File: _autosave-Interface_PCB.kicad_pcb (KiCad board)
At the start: 2 copper layers, 35 parts, among them IC1 STM32L412RBT6P, J1 USB_B, J2 AVR-JTAG-10, J3 Conn_01x04, J4 Conn_01x04, J5 Conn_01x04, J6 Conn_01x04, J7 Micro_SD_Card, U1 AMS1117-3.3

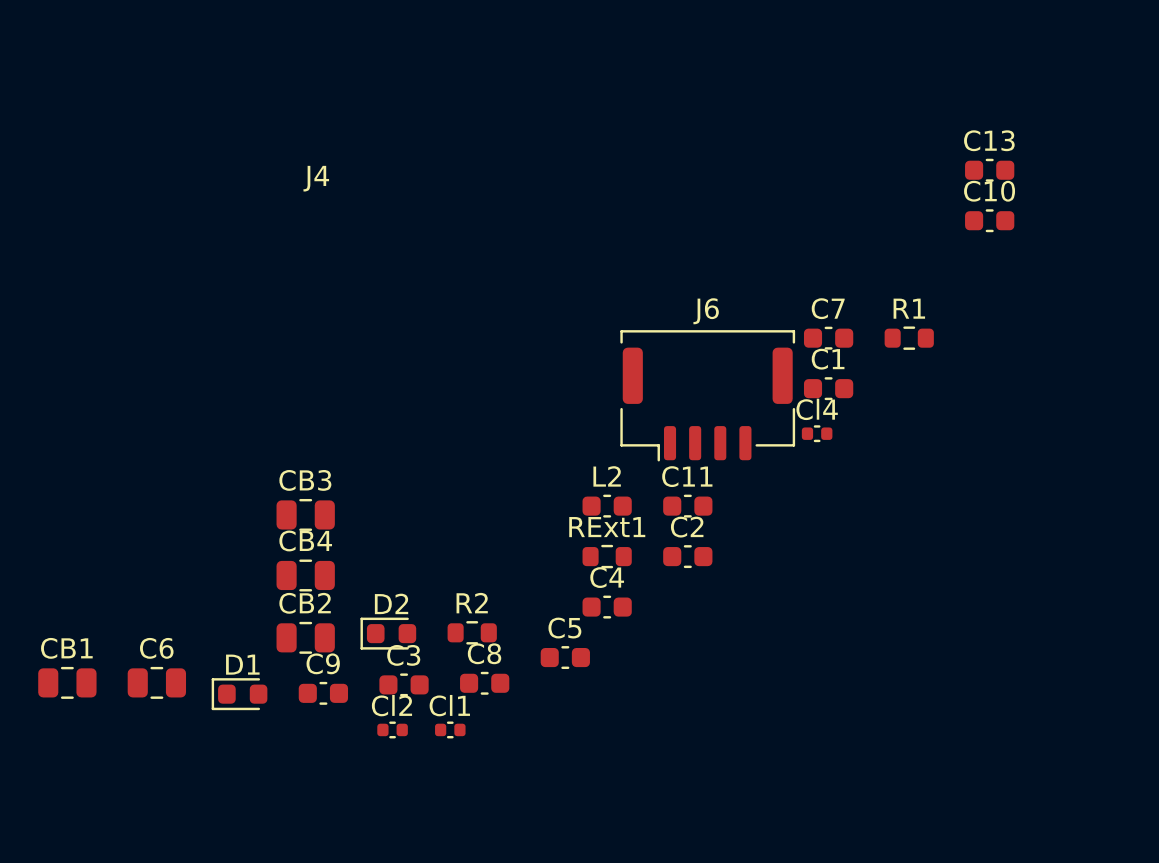
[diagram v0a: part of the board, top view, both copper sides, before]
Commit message: README added
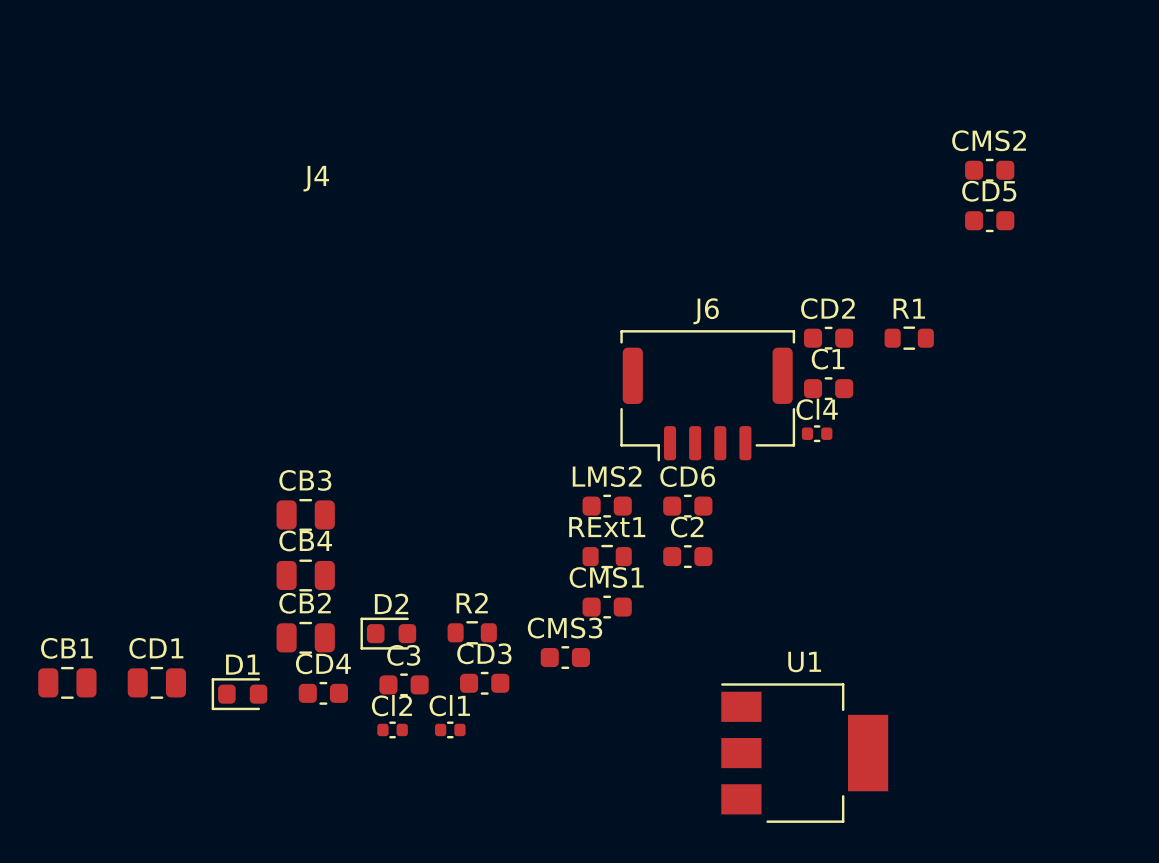
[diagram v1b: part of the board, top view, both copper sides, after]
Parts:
- added U1: AMS1117-3.3, Package_TO_SOT_SMD:SOT-223-3_TabPin2, F.Cu at (99.1, 119.4)
- renumbered C6 to CD1, C7 to CD2, C8 to CD3, C9 to CD4, C10 to CD5, C11 to CD6, C4 to CMS1, C13 to CMS2, C5 to CMS3, L2 to LMS2

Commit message: Added all component links and modified the footprints
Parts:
- removed the U1 at (99.1, 119.4)
- added CD1: 4.7u, Capacitor_SMD:C_0402_1005Metric, F.Cu at (129.5, 106.7)
- added CD2: 100n, Capacitor_SMD:C_0805_2012Metric, F.Cu at (133.3, 109.4)
- added CD3: 100n, Capacitor_SMD:C_0805_2012Metric, F.Cu at (133.8, 106.4)
- added CD4: 100n, Capacitor_SMD:C_0805_2012Metric, F.Cu at (129.3, 109.4)
- added CD5: 100n, Capacitor_SMD:C_0805_2012Metric, F.Cu at (125.5, 115.2)
- added CD6: 100n, Capacitor_SMD:C_0805_2012Metric, F.Cu at (129.5, 114.5)
- added CMS1: 10n, Capacitor_SMD:C_0805_2012Metric, F.Cu at (137.8, 106.4)
- added CMS2: 1u, Capacitor_SMD:C_0805_2012Metric, F.Cu at (133.5, 112.0)
- added CMS3: 10n, Capacitor_SMD:C_0805_2012Metric, F.Cu at (129.5, 112.0)
- added CR1: 22uF, Capacitor_SMD:C_0402_1005Metric, F.Cu at (68.6, 58.4)
- added CR2: 22uF, Capacitor_SMD:C_0402_1005Metric, F.Cu at (65.7, 60.4)
- added CR3: 22uF, Capacitor_SMD:C_0402_1005Metric, F.Cu at (77.2, 54.9)
- added CSD1: 0.1uF, Capacitor_SMD:C_0402_1005Metric, F.Cu at (77.2, 56.8)
- added LMS1: 39nH, Capacitor_SMD:C_0603_1608Metric, F.Cu at (125.5, 112.7)
- added LR1: 39nH, Inductor_SMD:L_0402_1005Metric, F.Cu at (65.7, 58.4)
- added NT1: NetTie_3_Tee, NetTie:NetTie-3_SMD_Pad2.0mm, F.Cu at (70.0, 55.7)
- added Y1: Crystal, SamacSys_Parts:ABS05W32768KHZD2T, F.Cu at (121.2, 113.5)
- added Y2: Crystal, SamacSys_Parts:ECS80830QVSTR, F.Cu at (122.8, 108.3)
- CB1, CB2, CB3: footprint Capacitor_SMD:C_0805_2012Metric -> Capacitor_SMD:C_0402_1005Metric
- D1, D2: footprint LED_SMD:LED_0603_1608Metric -> LED_SMD:LED_0805_2012Metric
- IC1: footprint STM32L412RBT6P:QFP50P1200X1200X160-64N -> SamacSys_Parts:QFP50P1200X1200X160-64N
- J1: value USB_B -> Conn_01x04; footprint Connector_USB:USB_Micro-B_Amphenol_10104110_Horizontal -> SamacSys_Parts:502382-0470
- J2: value AVR-JTAG-10 -> Conn_01x04; footprint Connector_PinHeader_2.54mm:PinHeader_2x05_P2.54mm_Vertical_SMD -> SamacSys_Parts:502382-0470
- J3, J4: footprint Connector_Molex:Molex_CLIK-Mate_502382-0470_1x04-1MP_P1.25mm_Vertical -> SamacSys_Parts:502382-0470
- J5: value Conn_01x04 -> AVR-JTAG-10; footprint Connector_Molex:Molex_CLIK-Mate_502382-0470_1x04-1MP_P1.25mm_Vertical -> Connector_PinHeader_2.54mm:PinHeader_2x05_P2.54mm_Vertical_SMD
- J6: value Conn_01x04 -> Micro_SD_Card; footprint Connector_Molex:Molex_CLIK-Mate_502382-0470_1x04-1MP_P1.25mm_Vertical -> SamacSys_Parts:693072010801
- J7: value Micro_SD_Card -> USB_B; footprint Connector_Card:microSD_HC_Wuerth_693072010801 -> SamacSys_Parts:GMCB05B11124H1EU
- R1, R2: footprint Resistor_SMD:R_0603_1608Metric -> Resistor_SMD:R_0805_2012Metric
- moved IC1 82.0 mm to (210.8, 48.3)
- moved J2 33.4 mm to (121.9, 61.0)
- moved J5 21.7 mm to (124.4, 35.6)
- moved J3 10.5 mm to (170.2, 81.3)
- moved J4 9.16 mm to (137.2, 76.2)
- renumbered CD5 to C10, CD6 to C11, CMS2 to C13, CMS1 to C4, CMS3 to C5, CD1 to C6, CD2 to C7, CD3 to C8, CD4 to C9, LMS2 to L2
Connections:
- Cl1 pad 1: LSE_IN -> LSE_OUT
- Cl2 pad 1: LSE_OUT -> LSE_IN
- J1 pad 1: VBUS -> GND
- J1 pad 2: USB_D- -> I2C1_SDA
- J1 pad 3: USB_D+ -> I2C1_SCL
- J1 pad 4: GND -> +3V3
- J1 pad 5: unconnected-(J1-Pad5) -> (no net)
- J2 pad 1: JTCK -> GND
- J2 pad 2: GND -> USART1_RX
- J2 pad 3: JTDO -> USART1_TX
- J2 pad 5: JTMS -> (no net)
- J2 pad 6: unconnected-(J2-Pad6) -> (no net)
- J3 pad 2: I2C1_SDA -> I2C2_SCL
- J3 pad 3: I2C1_SCL -> I2C2_SDA
- J4 pad 2: I2C2_SCL -> USART2_RX
- J4 pad 3: I2C2_SDA -> USART2_TX
- J5 pad 1: GND -> JTCK
- J5 pad 2: USART1_RX -> GND
- J5 pad 3: USART1_TX -> JTDO
- J6 pad 1: GND -> unconnected-(J6-Pad1)
- J6 pad 2: USART2_RX -> CS
- J6 pad 3: USART2_TX -> SPI1_MOSI
- J7 pad 1: unconnected-(J7-Pad1) -> VBUS
- J7 pad 2: CS -> USB_D-
- J7 pad 3: SPI1_MOSI -> USB_D+
- J7 pad 4: +3V3 -> GND
- J7 pad 5: CLK -> unconnected-(J7-Pad5)
- U1 pad 1: GND -> Net-(CR1-Pad2)
- U1 pad 2: Net-(C3-Pad1) -> +3V3
- U1 pad 3: Net-(C2-Pad1) -> Net-(CR1-Pad1)
